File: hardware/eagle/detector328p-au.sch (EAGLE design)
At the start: 66 parts, among them K1 SRD-05VDC-SL-C, Q1 BSS123, Q2 16MHz, T1 BC817, T2 BC817, T3 BC817, U1 ATMEGA328P-AU

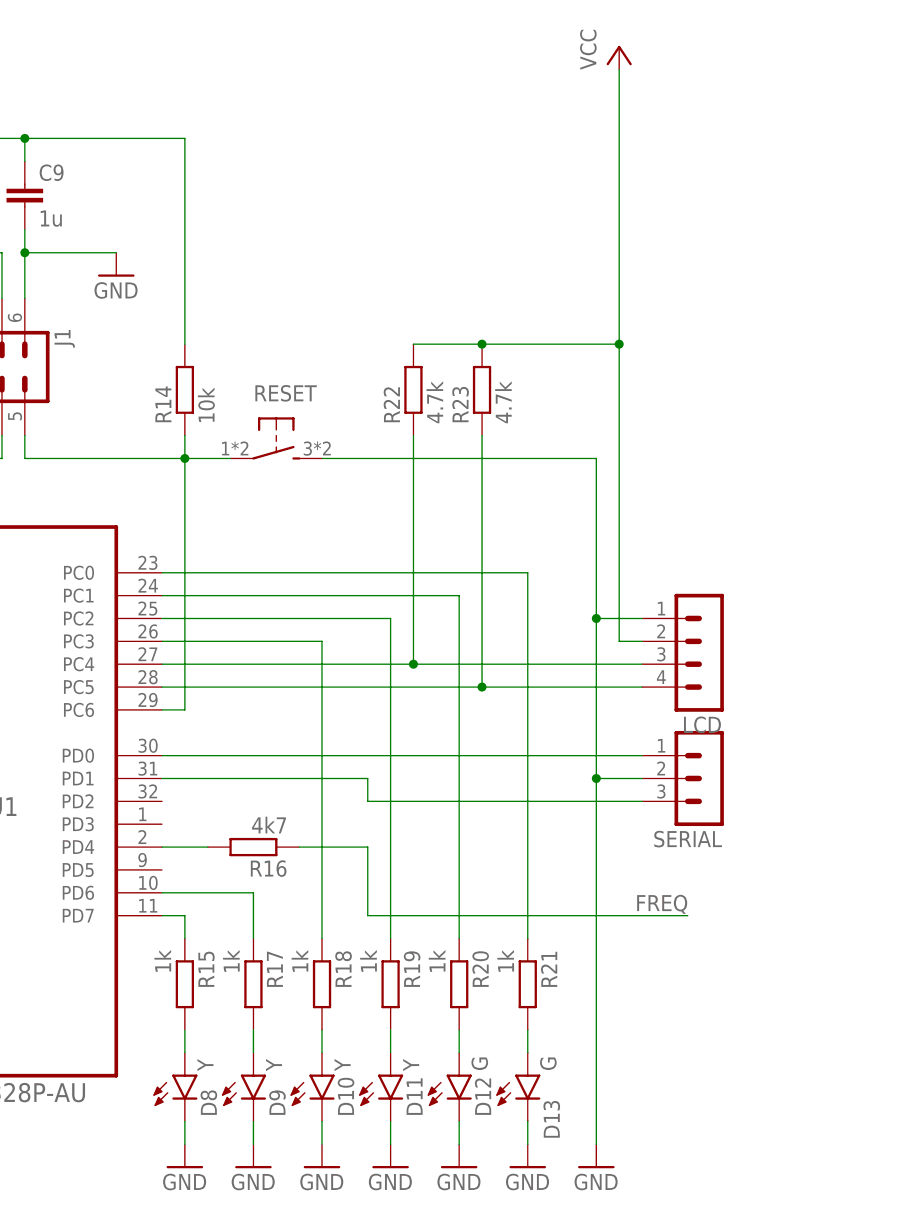
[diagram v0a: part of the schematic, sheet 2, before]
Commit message: hardware/eagle: added 3 push buttons
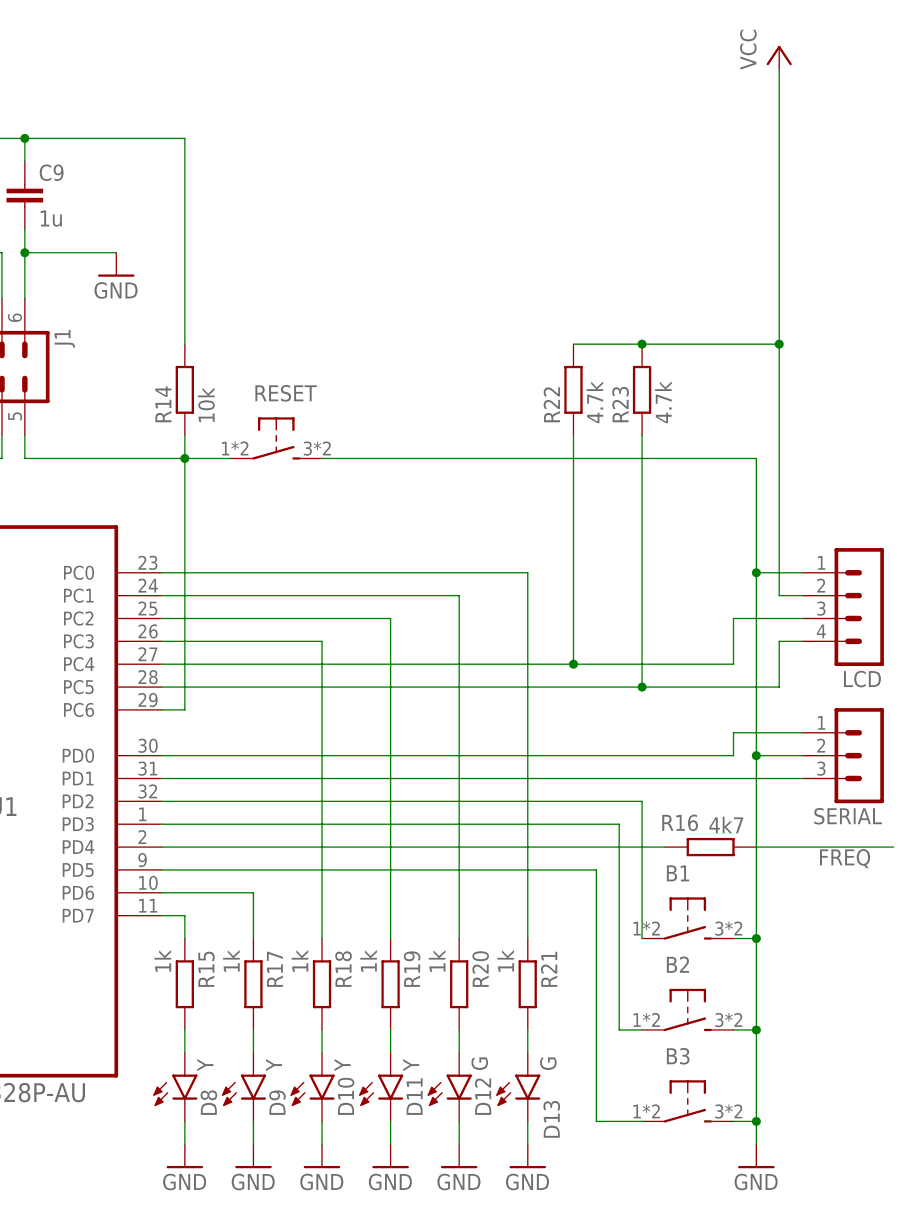
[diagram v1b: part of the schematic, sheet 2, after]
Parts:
- added B1, B2, B3: (no value), detector:10-XX
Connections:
- new net N$49: B1.P, U1.PD2
- new net N$50: B2.P, U1.PD3
- new net N$51: B3.P, U1.PD5
- net GND: now also B1.S, B2.S, B3.S
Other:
- moved on the sheet: LCD, R16, R22, R23, SERIAL

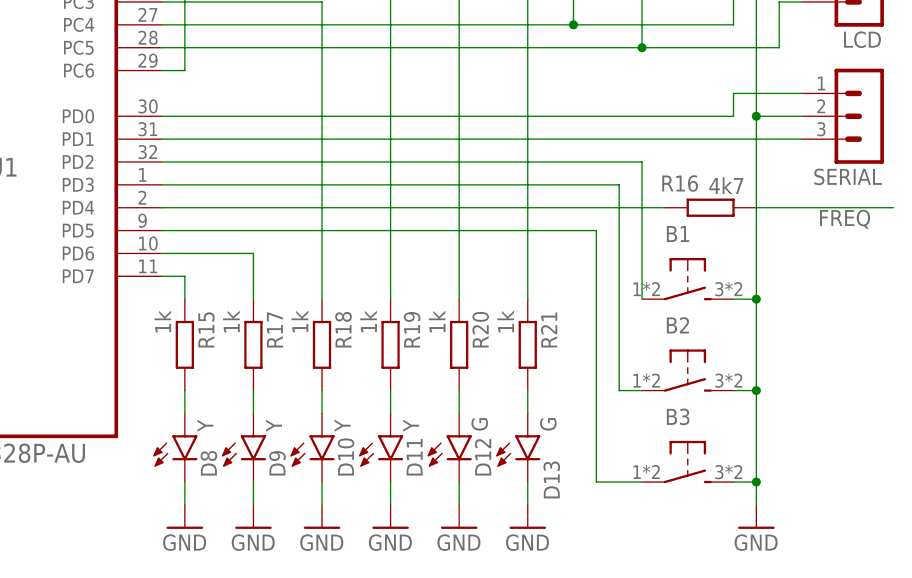
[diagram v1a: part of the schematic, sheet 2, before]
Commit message: CarDetector v1.1 hardware (3 more button)
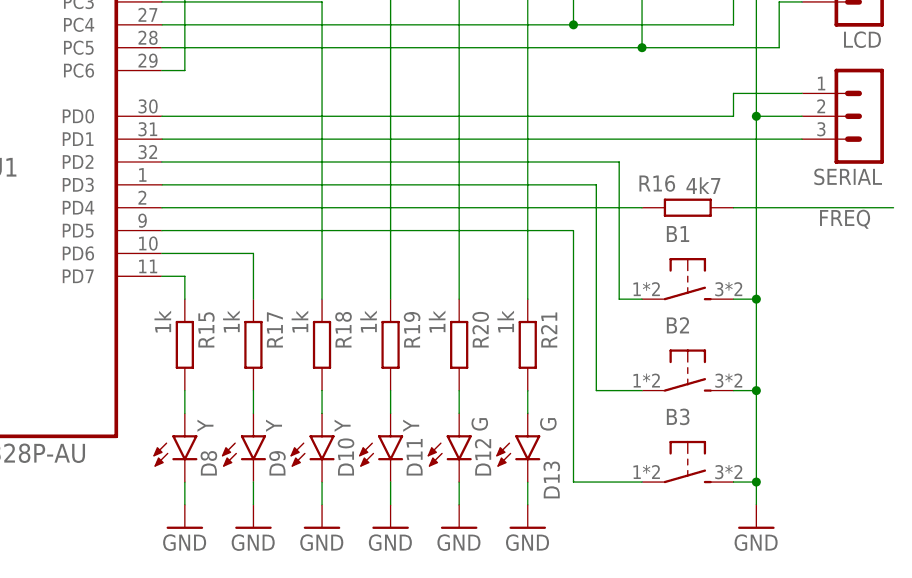
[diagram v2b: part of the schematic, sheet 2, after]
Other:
- moved on the sheet: R16
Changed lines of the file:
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@@
 <?xml version="1.0" encoding="utf-8"?>
 <!DOCTYPE eagle SYSTEM "eagle.dtd">
-<eagle version="7.6.0">
+<eagle version="7.1.0">
 <drawing>
 <settings>
@@
 <attribute name="VALUE" x="106.8832" y="17.399" size="2.0828" layer="96" ratio="10" rot="SR0"/>
 </instance>
-<instance part="R16" gate="G$1" x="198.12" y="45.72" smashed="yes" rot="R180">
-<attribute name="NAME" x="196.85" y="49.3014" size="1.778" layer="95" rot="R180"/>
-<attribute name="VALUE" x="201.93" y="49.022" size="1.778" layer="96" rot="R180"/>
+<instance part="R16" gate="G$1" x="195.58" y="45.72" smashed="yes" rot="R180">
+<attribute name="NAME" x="194.31" y="49.3014" size="1.778" layer="95" rot="R180"/>
+<attribute name="VALUE" x="199.39" y="49.022" size="1.778" layer="96" rot="R180"/>
 </instance>
 <instance part="GND16" gate="1" x="88.9" y="10.16"/>
@@
 <pinref part="R16" gate="G$1" pin="2"/>
 <pinref part="U1" gate="A" pin="PD4"/>
-<wire x1="193.04" y1="45.72" x2="137.16" y2="45.72" width="0.1524" layer="91"/>
+<wire x1="190.5" y1="45.72" x2="137.16" y2="45.72" width="0.1524" layer="91"/>
 </segment>
 </net>
@@
 <segment>
 <pinref part="R16" gate="G$1" pin="1"/>
-<wire x1="203.2" y1="45.72" x2="218.44" y2="45.72" width="0.1524" layer="91"/>
+<wire x1="200.66" y1="45.72" x2="218.44" y2="45.72" width="0.1524" layer="91"/>
 <label x="210.058" y="43.688" size="1.778" layer="95"/>
 </segment>
@@
 <pinref part="U1" gate="A" pin="PD2"/>
 <pinref part="B1" gate="1" pin="P"/>
-<wire x1="137.16" y1="50.8" x2="190.5" y2="50.8" width="0.1524" layer="91"/>
-<wire x1="190.5" y1="50.8" x2="190.5" y2="35.56" width="0.1524" layer="91"/>
+<wire x1="137.16" y1="50.8" x2="187.96" y2="50.8" width="0.1524" layer="91"/>
+<wire x1="187.96" y1="50.8" x2="187.96" y2="35.56" width="0.1524" layer="91"/>
+<wire x1="187.96" y1="35.56" x2="190.5" y2="35.56" width="0.1524" layer="91"/>
 </segment>
 </net>
@@
 <segment>
 <pinref part="U1" gate="A" pin="PD3"/>
-<wire x1="137.16" y1="48.26" x2="187.96" y2="48.26" width="0.1524" layer="91"/>
-<wire x1="187.96" y1="48.26" x2="187.96" y2="25.4" width="0.1524" layer="91"/>
+<wire x1="137.16" y1="48.26" x2="185.42" y2="48.26" width="0.1524" layer="91"/>
+<wire x1="185.42" y1="48.26" x2="185.42" y2="25.4" width="0.1524" layer="91"/>
 <pinref part="B2" gate="1" pin="P"/>
-<wire x1="187.96" y1="25.4" x2="190.5" y2="25.4" width="0.1524" layer="91"/>
+<wire x1="185.42" y1="25.4" x2="190.5" y2="25.4" width="0.1524" layer="91"/>
 </segment>
 </net>
@@
 <segment>
 <pinref part="U1" gate="A" pin="PD5"/>
-<wire x1="137.16" y1="43.18" x2="185.42" y2="43.18" width="0.1524" layer="91"/>
-<wire x1="185.42" y1="43.18" x2="185.42" y2="15.24" width="0.1524" layer="91"/>
+<wire x1="137.16" y1="43.18" x2="182.88" y2="43.18" width="0.1524" layer="91"/>
+<wire x1="182.88" y1="43.18" x2="182.88" y2="15.24" width="0.1524" layer="91"/>
 <pinref part="B3" gate="1" pin="P"/>
-<wire x1="185.42" y1="15.24" x2="190.5" y2="15.24" width="0.1524" layer="91"/>
-</segment>
-</net>
+<wire x1="182.88" y1="15.24" x2="190.5" y2="15.24" width="0.1524" layer="91"/>
+</segment>
+</net>

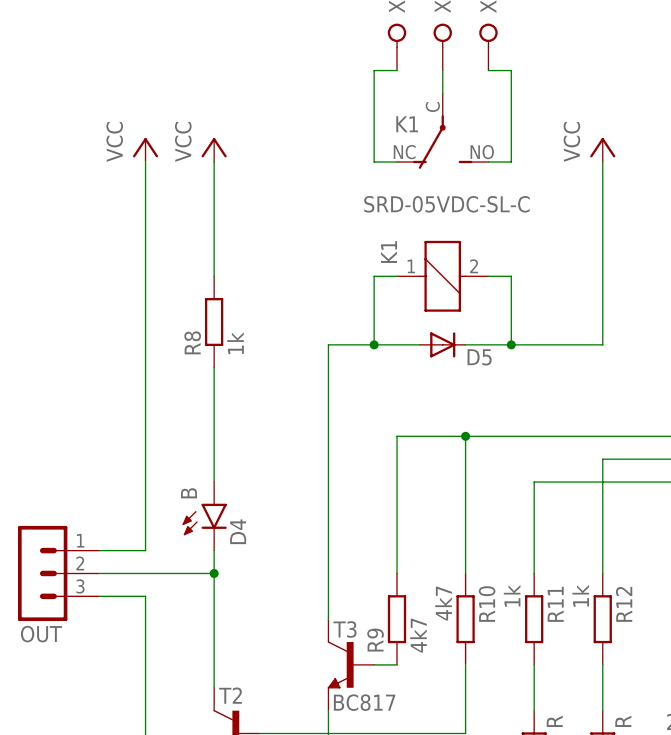
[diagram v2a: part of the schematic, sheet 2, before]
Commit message: Fix: detector_t85-pu: T2 10K pull-up, Zener 5,1V -> 20V
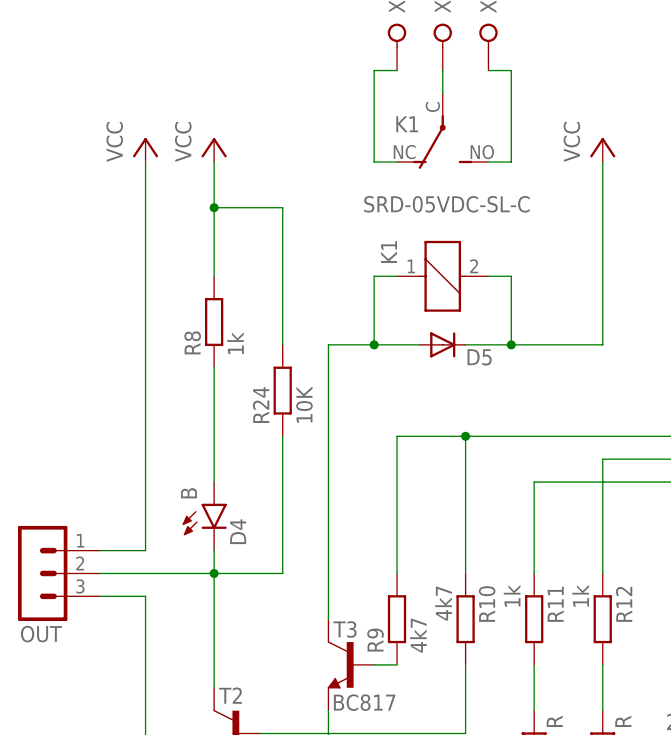
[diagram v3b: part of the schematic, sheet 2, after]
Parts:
- added R24: 10K, resistor:R-EU_R0603
- D1, D2: value 5.1V 0.5W -> 20V 0.5W
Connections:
- net N$23: now also R24.1
- net VCC: now also R24.2
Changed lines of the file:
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@@
 <part name="R4" library="resistor" deviceset="R-EU_" device="R0603" value="150"/>
 <part name="GND6" library="supply1" deviceset="GND" device=""/>
-<part name="D1" library="diode" deviceset="ZENER-DIODE" device="SOD80C" value="5.1V 0.5W"/>
-<part name="D2" library="diode" deviceset="ZENER-DIODE" device="SOD80C" value="5.1V 0.5W"/>
+<part name="D1" library="diode" deviceset="ZENER-DIODE" device="SOD80C" value="20V 0.5W"/>
+<part name="D2" library="diode" deviceset="ZENER-DIODE" device="SOD80C" value="20V 0.5W"/>
 <part name="GND-ISO1" library="SparkFun-Aesthetics" deviceset="GND-ISO" device=""/>
 <part name="R1" library="resistor" deviceset="R-EU_" device="R0603" value="1M8"/>
@@
 <part name="B2" library="detector" deviceset="10-XX" device=""/>
 <part name="B3" library="detector" deviceset="10-XX" device=""/>
+<part name="R24" library="resistor" deviceset="R-EU_" device="R0603" value="10K"/>
 </parts>
 <sheets>
@@
 <instance part="B2" gate="1" x="195.58" y="25.4" rot="R270"/>
 <instance part="B3" gate="1" x="195.58" y="15.24" rot="R270"/>
+<instance part="R24" gate="G$1" x="25.4" y="58.42" rot="R90"/>
 </instances>
 <busses>
@@
 <pinref part="R8" gate="G$1" pin="2"/>
 <pinref part="P+5" gate="VCC" pin="VCC"/>
-<wire x1="17.78" y1="71.12" x2="17.78" y2="83.82" width="0.1524" layer="91"/>
+<wire x1="17.78" y1="71.12" x2="17.78" y2="78.74" width="0.1524" layer="91"/>
+<pinref part="R24" gate="G$1" pin="2"/>
+<wire x1="17.78" y1="78.74" x2="17.78" y2="83.82" width="0.1524" layer="91"/>
+<wire x1="25.4" y1="63.5" x2="25.4" y2="78.74" width="0.1524" layer="91"/>
+<wire x1="25.4" y1="78.74" x2="17.78" y2="78.74" width="0.1524" layer="91"/>
+<junction x="17.78" y="78.74"/>
 </segment>
 <segment>
@@
 <wire x1="5.08" y1="38.1" x2="17.78" y2="38.1" width="0.1524" layer="91"/>
 <junction x="17.78" y="38.1"/>
-</segment>
-</net>
+<pinref part="R24" gate="G$1" pin="1"/>
+<wire x1="17.78" y1="38.1" x2="25.4" y2="38.1" width="0.1524" layer="91"/>
+<wire x1="25.4" y1="38.1" x2="25.4" y2="53.34" width="0.1524" layer="91"/>
+</segment>
+</net>
